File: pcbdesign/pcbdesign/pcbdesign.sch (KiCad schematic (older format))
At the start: 32 parts, among them J1 Conn_01x06_Male, J2 USB_B_Micro, J3 Conn_Coaxial, SW1 SW_Push, SW2 SW_Push, U1 CMWX1ZZABZ-078, U2 LM1117ADJ

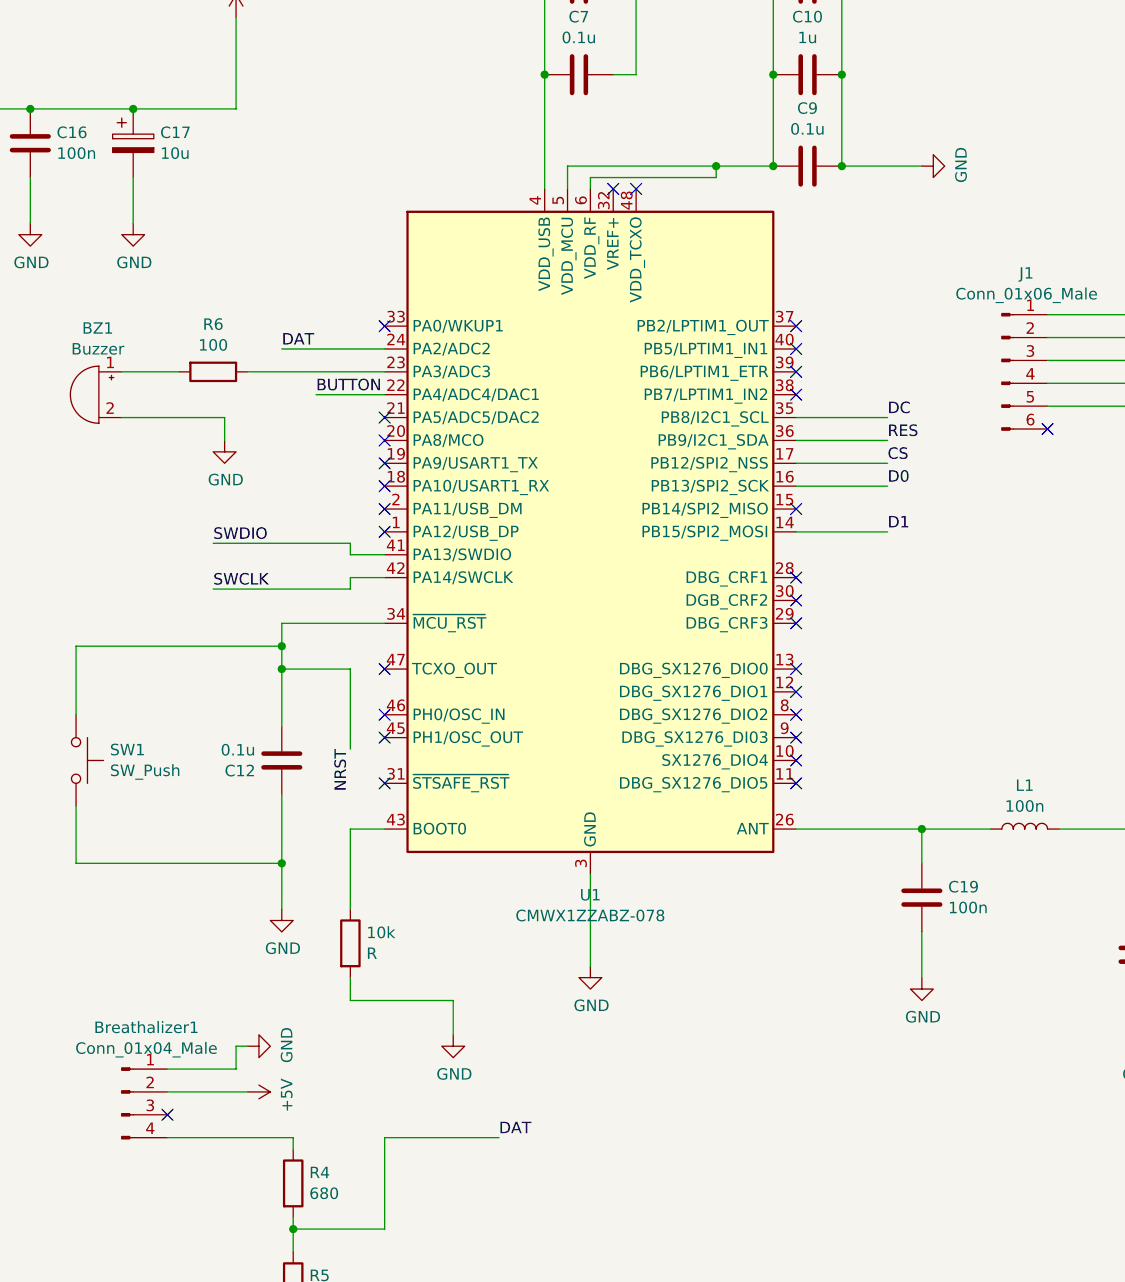
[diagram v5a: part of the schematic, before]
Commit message: Update PCB schematic to include the missing wires
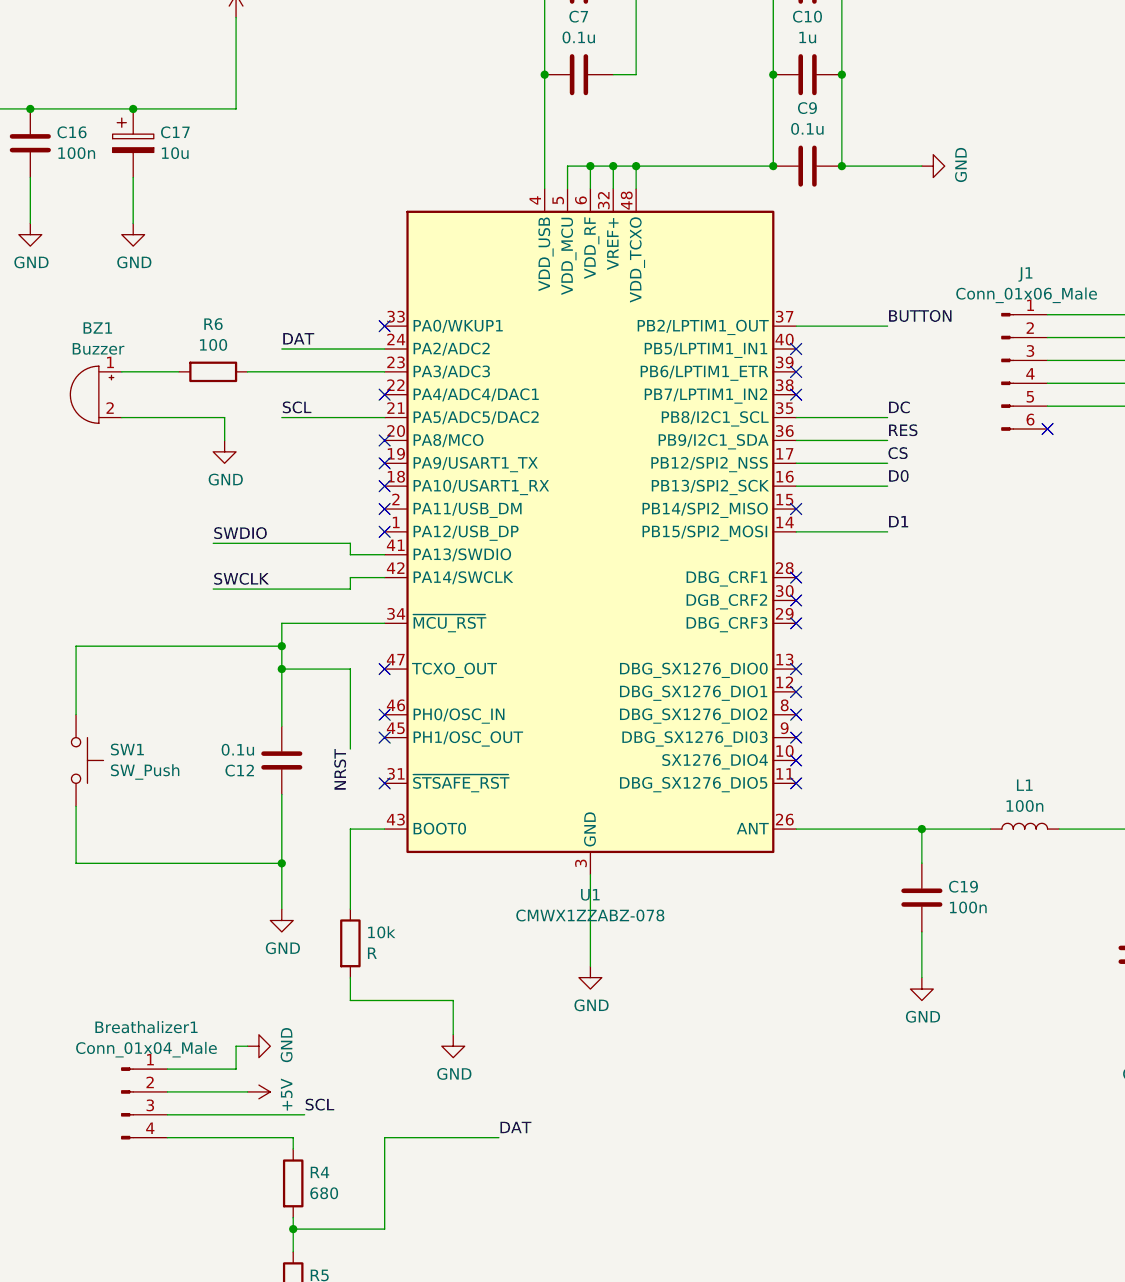
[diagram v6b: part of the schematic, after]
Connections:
- net +3V3: now also U1.32 (VREF+), U1.48 (VDD_TCXO)
- net BUTTON: now also U1.37 (PB2/LPTIM1_OUT); no longer U1.22 (PA4/ADC4/DAC1)
- net SCL: now reaches U1.21 (PA5/ADC5/DAC2)
- net SCL: now also Breathalizer1.3 (Pin_3)
- no-connect marks 32 -> 28
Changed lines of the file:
@@
 	7300 2050 7300 1950
-Wire Wire Line
-	7300 1950 7950 1950
-Wire Wire Line
-	7400 2050 7400 2000
-Wire Wire Line
-	7400 2000 7950 2000
-Wire Wire Line
-	7950 2000 7950 1950
-Connection ~ 7950 1950
-Wire Wire Line
-	7950 1950 8200 1950
 Wire Wire Line
 	8200 1950 8200 1550
@@
 NoConn ~ 8300 2850
 NoConn ~ 8300 2750
-NoConn ~ 8300 2650
-NoConn ~ 7500 2050
-NoConn ~ 7600 2050
 $Comp
 L Connector:Conn_01x04_Male Breathalizer1
@@
 	0    -1   -1   0
 $EndComp
-NoConn ~ 5550 6100
 Text Label 7000 6200 0    50   ~ 0
 DAT
@@
 Wire Wire Line
 	8300 3550 8700 3550
-NoConn ~ 6500 3050
 Text Label 8700 3050 0    50   ~ 0
 DC
@@
 Text Label 3200 3350 0    50   ~ 0
 BUTTON
-Text Label 6200 2950 0    50   ~ 0
-BUTTON
-Wire Wire Line
-	6500 2950 6200 2950
 $Comp
 L pcbdesign-rescue:CMWX1ZZABZ-078-cmwx1zzabz-078 U1
@@
 Wire Wire Line
 	6800 5600 6800 5750
+Text Label 8700 2650 0    50   ~ 0
+BUTTON
+Wire Wire Line
+	8300 2650 8700 2650
+NoConn ~ 6500 2950
+Wire Wire Line
+	7300 1950 7400 1950
+Wire Wire Line
+	7400 1950 7400 2050
+Connection ~ 7400 1950
+Wire Wire Line
+	7400 1950 7500 1950
+Wire Wire Line
+	7500 2050 7500 1950
+Connection ~ 7500 1950
+Wire Wire Line
+	7500 1950 7600 1950
+Wire Wire Line
+	7600 2050 7600 1950
+Connection ~ 7600 1950
+Wire Wire Line
+	7600 1950 8200 1950
+Text Label 6150 6100 0    50   ~ 0
+SCL
+Wire Wire Line
+	5550 6100 6150 6100
+Text Label 6050 3050 0    50   ~ 0
+SCL
+Wire Wire Line
+	6050 3050 6500 3050
 $EndSCHEMATC

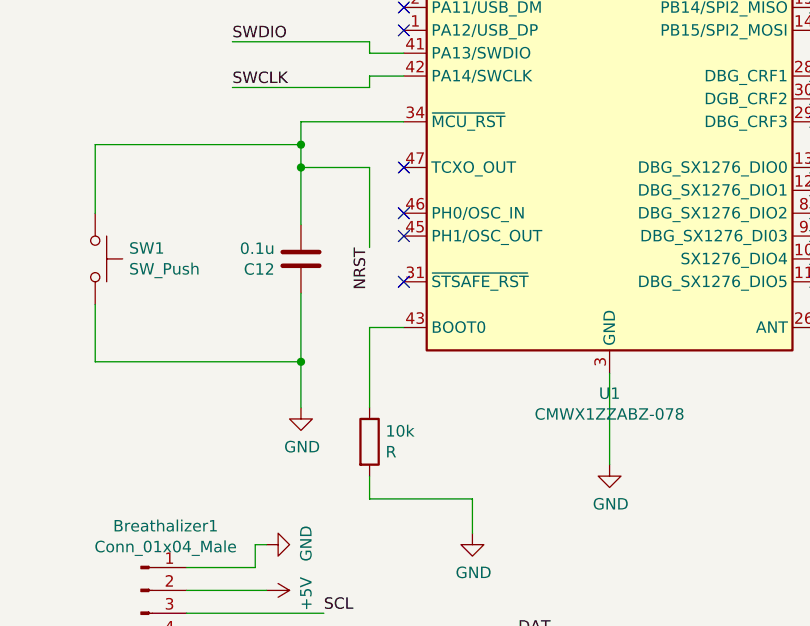
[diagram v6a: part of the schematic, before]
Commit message: Add wire for LoRa crystal, annotate forgotten resistor
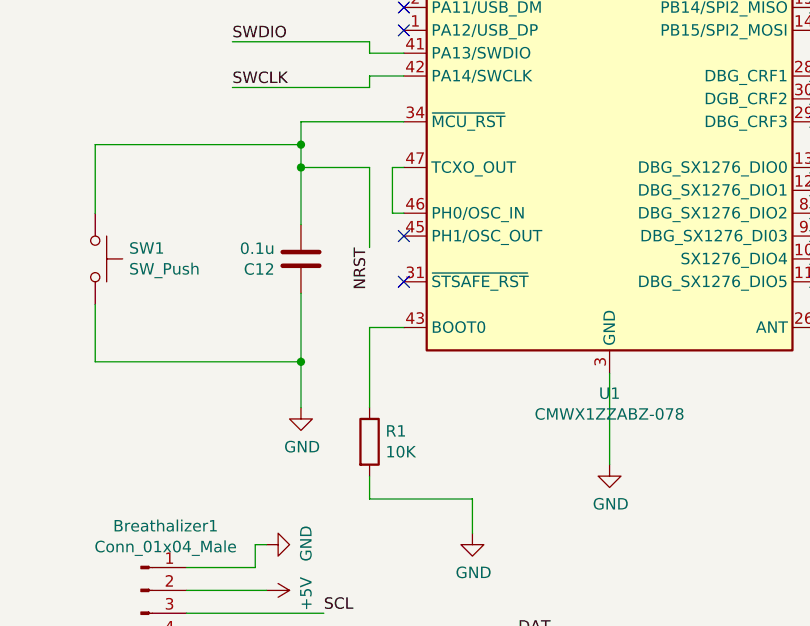
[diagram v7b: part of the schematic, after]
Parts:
- R1: renamed from 10k; value R -> 10K
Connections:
- net at U1.46 (PH0/OSC_IN): now also U1.47 (TCXO_OUT)
- no-connect marks 28 -> 26
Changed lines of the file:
@@
 NoConn ~ 6500 3450
 NoConn ~ 6500 3550
-NoConn ~ 6500 4150
-NoConn ~ 6500 4350
 NoConn ~ 6500 4450
 NoConn ~ 6500 4650
@@
 $EndComp
 $Comp
-L power:GND #PWR?
+L power:GND #PWR0102
 U 1 1 5E596E1C
 P 6800 5750
-F 0 "#PWR?" H 6800 5500 50  0001 C CNN
+F 0 "#PWR0102" H 6800 5500 50  0001 C CNN
 F 1 "GND" H 6805 5577 50  0000 C CNN
 F 2 "" H 6800 5750 50  0001 C CNN
@@
 $EndComp
 $Comp
-L Device:R 10k
+L Device:R R1
 U 1 1 5E5A6329
 P 6350 5350
-F 0 "10k" H 6420 5396 50  0000 L CNN
-F 1 "R" H 6420 5305 50  0000 L CNN
+F 0 "R1" H 6420 5396 50  0000 L CNN
+F 1 "10K" H 6420 5305 50  0000 L CNN
 F 2 "" V 6280 5350 50  0001 C CNN
 F 3 "~" H 6350 5350 50  0001 C CNN
@@
 Wire Wire Line
 	6050 3050 6500 3050
+Wire Wire Line
+	6500 4150 6450 4150
+Wire Wire Line
+	6450 4150 6450 4350
+Wire Wire Line
+	6450 4350 6500 4350
 $EndSCHEMATC
